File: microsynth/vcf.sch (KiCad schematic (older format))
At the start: 45 parts, among them Q4 BC212 PNP, Q5 BC212 PNP, Q6 BC548, Q7 BC548, Q8 BC548, SW10 SW_SPST, SW11 SW_SPDT, U19 LM741, U20 LM13600

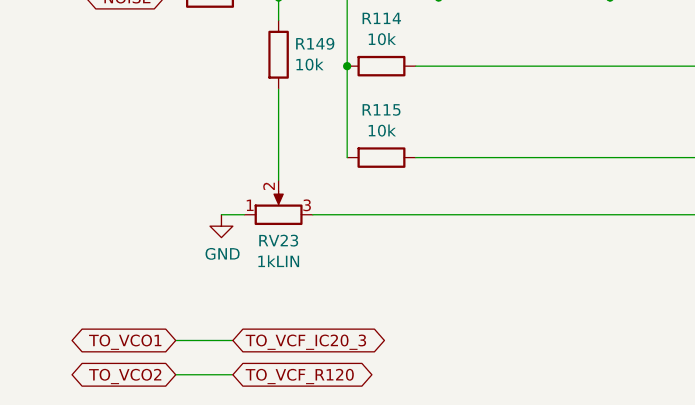
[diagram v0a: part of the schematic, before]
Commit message: Label pots
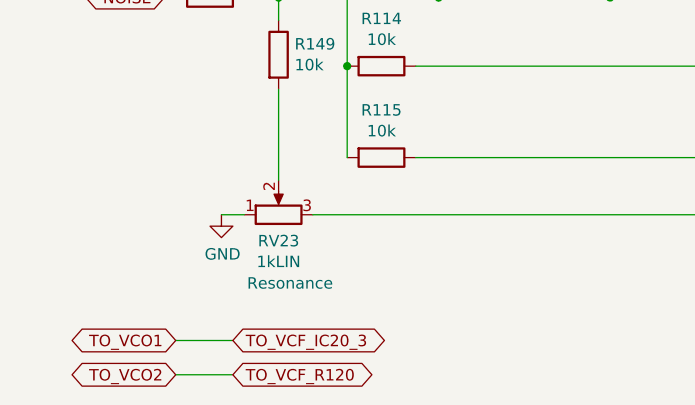
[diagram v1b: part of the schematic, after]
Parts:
- RV23: Label (none) -> Resonance
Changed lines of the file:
@@
 F 2 "4ms_Potentiometer:Pot_16mm_NoDet_RV16AF-4A" H 1550 6450 50  0001 C CNN
 F 3 "~" H 1550 6450 50  0001 C CNN
+F 4 "Resonance" V 1250 6400 50  0000 C CNN "Label"
 	1    1550 6450
 	0    -1   -1   0

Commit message: Replace dodgy parts 1458, 4136 & LF351s
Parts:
- U20: footprint Package_DIP:DIP-16_W7.62mm -> Package_DIP:DIP-16_W7.62mm_LongPads
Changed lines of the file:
@@
 F 0 "U20" H 4700 4433 50  0000 C CNN
 F 1 "LM13600" H 4700 4524 50  0000 C CNN
-F 2 "Package_DIP:DIP-16_W7.62mm" H 4400 4825 50  0001 C CNN
+F 2 "Package_DIP:DIP-16_W7.62mm_LongPads" H 4400 4825 50  0001 C CNN
 F 3 "http://pdf.datasheetcatalog.com/datasheet/nationalsemiconductor/DS007980.PDF" H 4400 4825 50  0001 C CNN
 	1    4700 4800
@@
 F 0 "U20" H 2650 4433 50  0000 C CNN
 F 1 "LM13600" H 2650 4524 50  0000 C CNN
-F 2 "Package_DIP:DIP-16_W7.62mm" H 2350 4825 50  0001 C CNN
+F 2 "Package_DIP:DIP-16_W7.62mm_LongPads" H 2350 4825 50  0001 C CNN
 F 3 "http://pdf.datasheetcatalog.com/datasheet/nationalsemiconductor/DS007980.PDF" H 2350 4825 50  0001 C CNN
 	3    2650 4800
@@
 F 0 "U20" H 5400 5148 50  0000 C CNN
 F 1 "LM13600" H 5400 5057 50  0000 C CNN
-F 2 "Package_DIP:DIP-16_W7.62mm" H 5200 4825 50  0001 C CNN
+F 2 "Package_DIP:DIP-16_W7.62mm_LongPads" H 5200 4825 50  0001 C CNN
 F 3 "http://pdf.datasheetcatalog.com/datasheet/nationalsemiconductor/DS007980.PDF" H 5200 4825 50  0001 C CNN
 	2    5500 4800
@@
 F 0 "U20" H 3250 5148 50  0000 C CNN
 F 1 "LM13600" H 3250 5057 50  0000 C CNN
-F 2 "Package_DIP:DIP-16_W7.62mm" H 3050 4825 50  0001 C CNN
+F 2 "Package_DIP:DIP-16_W7.62mm_LongPads" H 3050 4825 50  0001 C CNN
 F 3 "http://pdf.datasheetcatalog.com/datasheet/nationalsemiconductor/DS007980.PDF" H 3050 4825 50  0001 C CNN
 	4    3350 4800
@@
 F 0 "U20" H 6408 4896 50  0000 L CNN
 F 1 "LM13600" H 6408 4805 50  0000 L CNN
-F 2 "Package_DIP:DIP-16_W7.62mm" H 6150 4875 50  0001 C CNN
+F 2 "Package_DIP:DIP-16_W7.62mm_LongPads" H 6150 4875 50  0001 C CNN
 F 3 "http://pdf.datasheetcatalog.com/datasheet/nationalsemiconductor/DS007980.PDF" H 6150 4875 50  0001 C CNN
 	5    6450 4850

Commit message: Consolidate switches
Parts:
- SW10, SW11: footprint Buttons_Switches_ThroughHole:GF-624-6014 -> microsynth:11-SS-22-701C
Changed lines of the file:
@@
 F 0 "SW10" H 1750 3275 50  0000 C CNN
 F 1 "SW_SPST" H 1750 3184 50  0000 C CNN
-F 2 "Buttons_Switches_ThroughHole:GF-624-6014" H 1750 2950 50  0001 C CNN
+F 2 "microsynth:11-SS-22-701C" H 1750 2950 50  0001 C CNN
 F 3 "~" H 1750 2950 50  0001 C CNN
 F 4 "VCF Keyboard Track" H 1750 3093 50  0000 C CNN "Label"
@@
 F 0 "SW11" H 4200 6925 50  0000 C CNN
 F 1 "SW_SPDT" H 4200 6834 50  0000 C CNN
-F 2 "Buttons_Switches_ThroughHole:GF-624-6014" H 4200 6550 50  0001 C CNN
+F 2 "microsynth:11-SS-22-701C" H 4200 6550 50  0001 C CNN
 F 3 "~" H 4200 6550 50  0001 C CNN
 F 4 "VCF MODE" H 4200 6743 50  0000 C CNN "Label"

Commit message: Consolidate all(?) switches
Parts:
- RV21, RV23, RV24: footprint 4ms_Potentiometer:Pot_16mm_NoDet_RV16AF-4A -> microsynth:Pot_16mm_NoDet_RV16AF-4A
- SW10: value SW_SPST -> SW_SPDT; symbol Switch:SW_SPST -> Switch:SW_SPDT
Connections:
- no-connect marks 3 -> 4
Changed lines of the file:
@@
 Wire Wire Line
 	2500 2800 2500 2950
-$Comp
-L Switch:SW_SPST SW10
-U 1 1 5E076B1B
-P 1750 2950
-F 0 "SW10" H 1750 3275 50  0000 C CNN
-F 1 "SW_SPST" H 1750 3184 50  0000 C CNN
-F 2 "microsynth:11-SS-22-701C" H 1750 2950 50  0001 C CNN
-F 3 "~" H 1750 2950 50  0001 C CNN
-F 4 "VCF Keyboard Track" H 1750 3093 50  0000 C CNN "Label"
-	1    1750 2950
-	1    0    0    -1
-$EndComp
 Wire Wire Line
 	1950 2950 2050 2950
@@
 F 0 "RV21" H 3330 1259 50  0000 R CNN
 F 1 "100kLIN" H 3330 1350 50  0000 R CNN
-F 2 "4ms_Potentiometer:Pot_16mm_NoDet_RV16AF-4A" H 3400 1350 50  0001 C CNN
+F 2 "microsynth:Pot_16mm_NoDet_RV16AF-4A" H 3400 1350 50  0001 C CNN
 F 3 "~" H 3400 1350 50  0001 C CNN
 F 4 "VCF Frequency" H 3330 1441 50  0000 R CNN "Label"
@@
 F 0 "RV23" V 1435 6450 50  0000 C CNN
 F 1 "1kLIN" V 1344 6450 50  0000 C CNN
-F 2 "4ms_Potentiometer:Pot_16mm_NoDet_RV16AF-4A" H 1550 6450 50  0001 C CNN
+F 2 "microsynth:Pot_16mm_NoDet_RV16AF-4A" H 1550 6450 50  0001 C CNN
 F 3 "~" H 1550 6450 50  0001 C CNN
 F 4 "Resonance" V 1250 6400 50  0000 C CNN "Label"
@@
 F 0 "RV24" H 7380 1509 50  0000 R CNN
 F 1 "10kLOG" H 7380 1600 50  0000 R CNN
-F 2 "4ms_Potentiometer:Pot_16mm_NoDet_RV16AF-4A" H 7450 1600 50  0001 C CNN
+F 2 "microsynth:Pot_16mm_NoDet_RV16AF-4A" H 7450 1600 50  0001 C CNN
 F 3 "~" H 7450 1600 50  0001 C CNN
 F 4 "Noise Level" H 7380 1691 50  0000 R CNN "Label"
@@
 	4550 6550 4400 6550
 Wire Wire Line
-	1450 2950 1550 2950
-Wire Wire Line
 	2950 3400 3600 3400
 Wire Wire Line
@@
 Text GLabel 1800 2650 0    50   BiDi ~ 0
 ENV_MOD
-Text GLabel 1450 2950 0    50   BiDi ~ 0
-KEYBOARD_IC7_PIN_6
 Text GLabel 1050 4700 0    50   BiDi ~ 0
 TO_VCO1
@@
 	-1   0    0    1
 $EndComp
+Text GLabel 1550 2850 0    50   BiDi ~ 0
+KEYBOARD_IC7_PIN_6
+$Comp
+L Switch:SW_SPDT SW10
+U 1 1 5E076B1B
+P 1750 2950
+F 0 "SW10" H 1750 2750 50  0000 C CNN
+F 1 "SW_SPDT" H 1750 2650 50  0000 C CNN
+F 2 "microsynth:11-SS-22-701C" H 1750 2950 50  0001 C CNN
+F 3 "~" H 1750 2950 50  0001 C CNN
+F 4 "VCF Keyboard Track" H 1750 2550 50  0000 C CNN "Label"
+	1    1750 2950
+	-1   0    0    -1
+$EndComp
+NoConn ~ 1550 3050
 $EndSCHEMATC

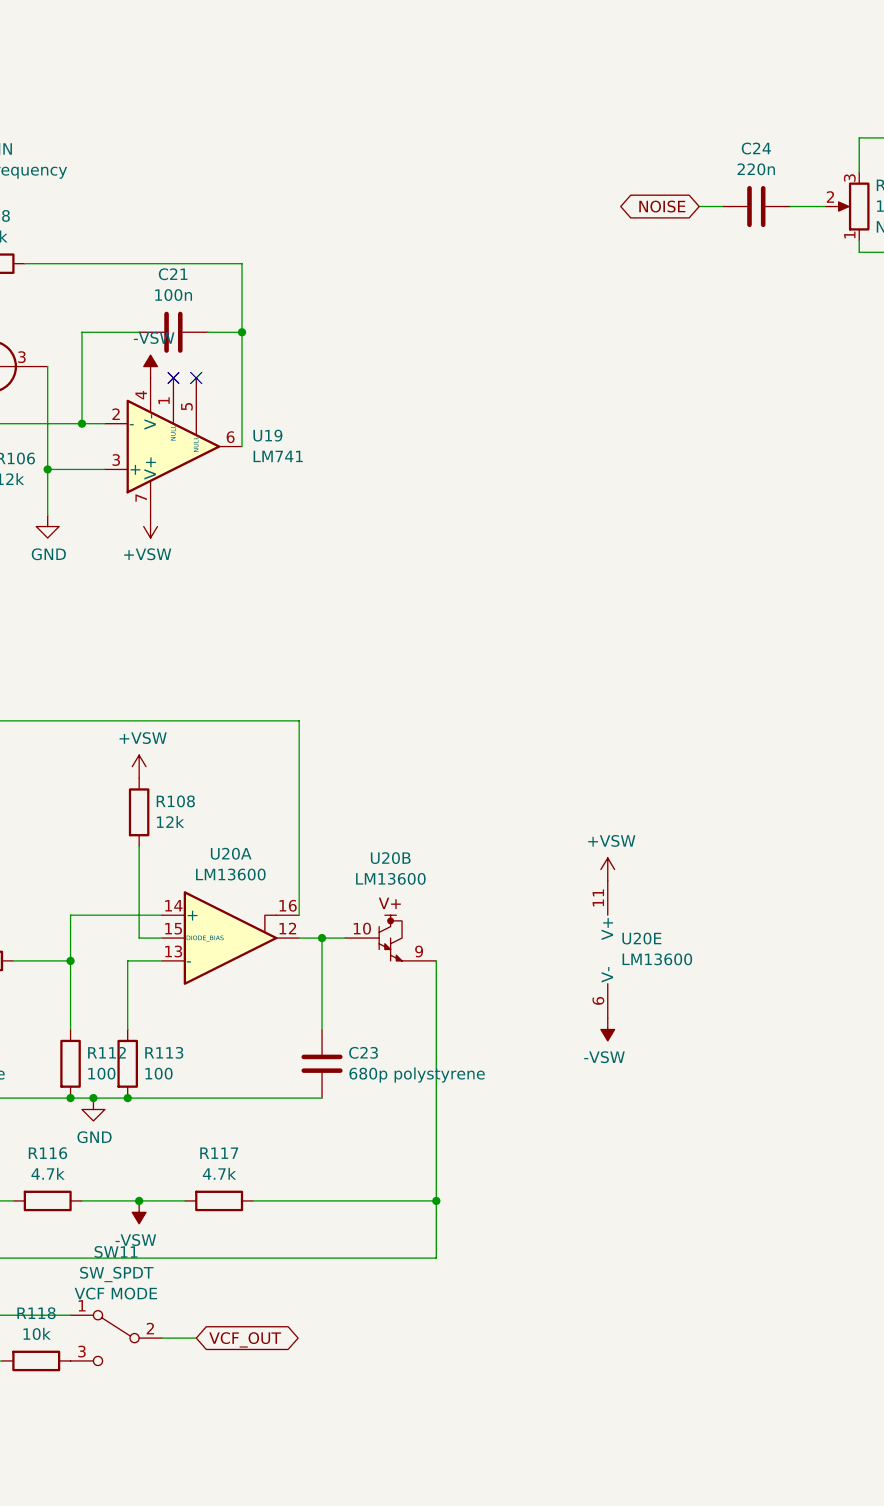
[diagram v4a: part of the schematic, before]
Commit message: Add test points
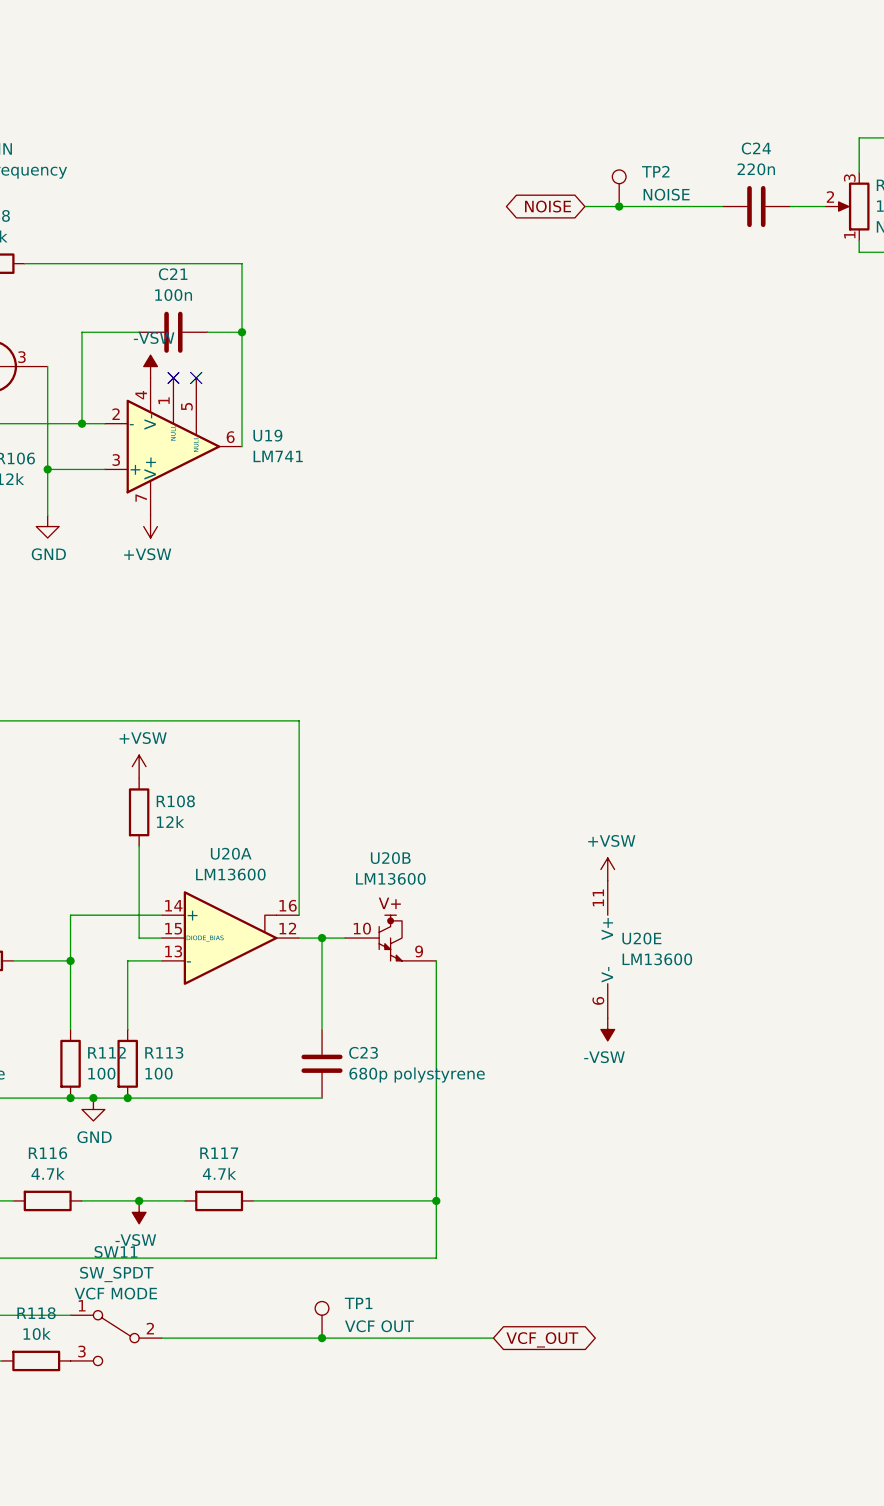
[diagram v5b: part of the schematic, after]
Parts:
- added TP1: VCF OUT, TestPoint:TestPoint_Pad_D2.0mm, symbol Connector:TestPoint
- added TP2: NOISE, TestPoint:TestPoint_Pad_D2.0mm, symbol Connector:TestPoint
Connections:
- net NOISE: now also TP2.1
- net VCF_OUT: now also TP1.1
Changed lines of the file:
@@
 $EndComp
 Wire Wire Line
-	6850 1600 6750 1600
+	6850 1600 6400 1600
 $Comp
 L Device:R_POT RV24
@@
 NoConn ~ 9800 1700
 Wire Wire Line
-	4550 6550 4400 6550
+	5850 6550 5100 6550
 Wire Wire Line
 	2950 3400 3600 3400
@@
 Text GLabel 1050 5500 0    50   BiDi ~ 0
 NOISE
-Text GLabel 6750 1600 0    50   BiDi ~ 0
+Text GLabel 6250 1600 0    50   BiDi ~ 0
 NOISE
-Text GLabel 4550 6550 2    50   BiDi ~ 0
+Text GLabel 5850 6550 2    50   BiDi ~ 0
 VCF_OUT
 Text GLabel 1250 900  0    50   BiDi ~ 0
@@
 $EndComp
 NoConn ~ 1550 3050
+$Comp
+L Connector:TestPoint TP?
+U 1 1 5EDF0D12
+P 5100 6550
+AR Path="/5E475532/5EDF0D12" Ref="TP?"  Part="1"
+AR Path="/5E05E45F/5EDF0D12" Ref="TP1"  Part="1"
+F 0 "TP1" H 5200 6700 50  0000 L CNN
+F 1 "VCF OUT" H 5200 6600 50  0000 L CNN
+F 2 "TestPoint:TestPoint_Pad_D2.0mm" H 5300 6550 50  0001 C CNN
+F 3 "~" H 5300 6550 50  0001 C CNN
+	1    5100 6550
+	1    0    0    -1
+$EndComp
+Connection ~ 5100 6550
+Wire Wire Line
+	5100 6550 4400 6550
+$Comp
+L Connector:TestPoint TP?
+U 1 1 5EDFC399
+P 6400 1600
+AR Path="/5E475532/5EDFC399" Ref="TP?"  Part="1"
+AR Path="/5E05E45F/5EDFC399" Ref="TP2"  Part="1"
+F 0 "TP2" H 6500 1750 50  0000 L CNN
+F 1 "NOISE" H 6500 1650 50  0000 L CNN
+F 2 "TestPoint:TestPoint_Pad_D2.0mm" H 6600 1600 50  0001 C CNN
+F 3 "~" H 6600 1600 50  0001 C CNN
+	1    6400 1600
+	1    0    0    -1
+$EndComp
+Connection ~ 6400 1600
+Wire Wire Line
+	6400 1600 6250 1600
 $EndSCHEMATC
